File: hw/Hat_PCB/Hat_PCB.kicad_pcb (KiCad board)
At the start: 4 copper layers, 65 x 56 mm, 18 parts, among them J3 40HAT, J6 CONN_02X02, J9 CONN_01X02, Q1 DMG2305UX, Q2 DMMT5401, U2 CAT24C32

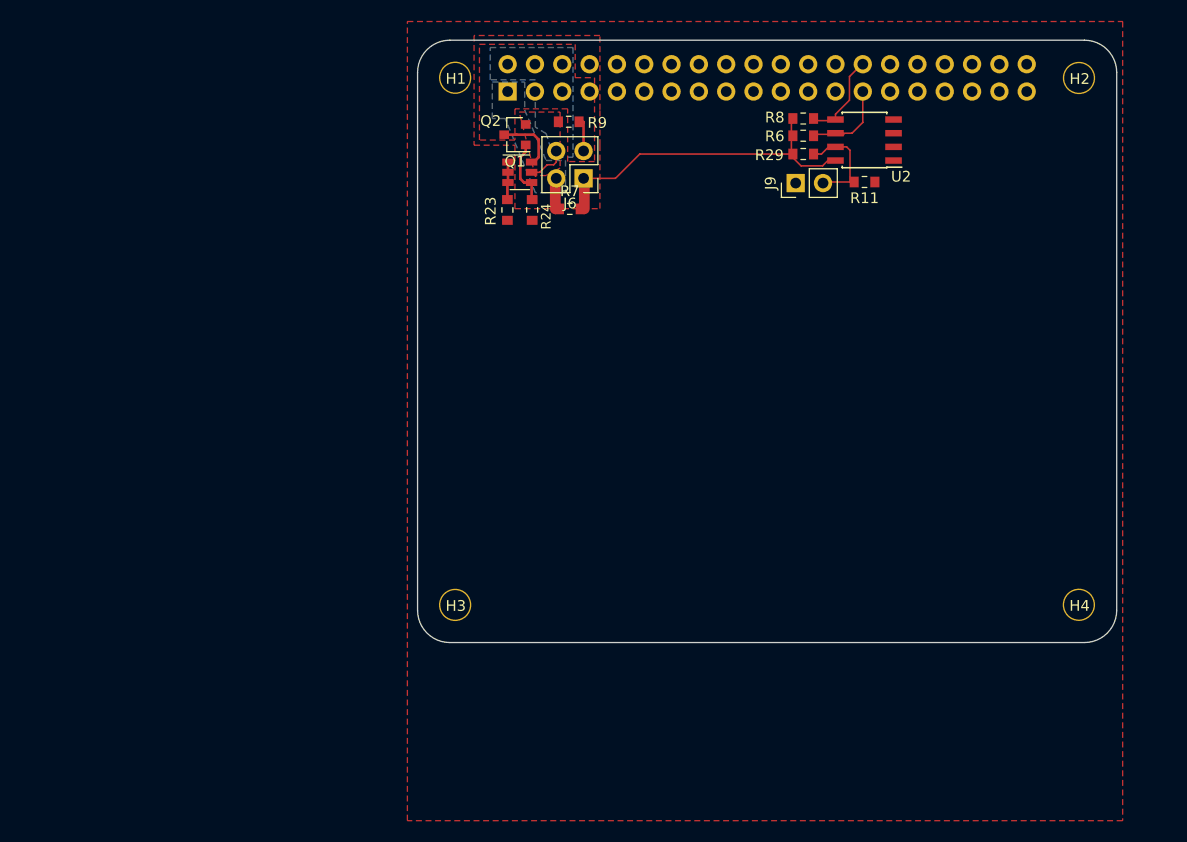
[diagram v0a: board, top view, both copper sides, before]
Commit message: Schematic mostly done, started prelim layout
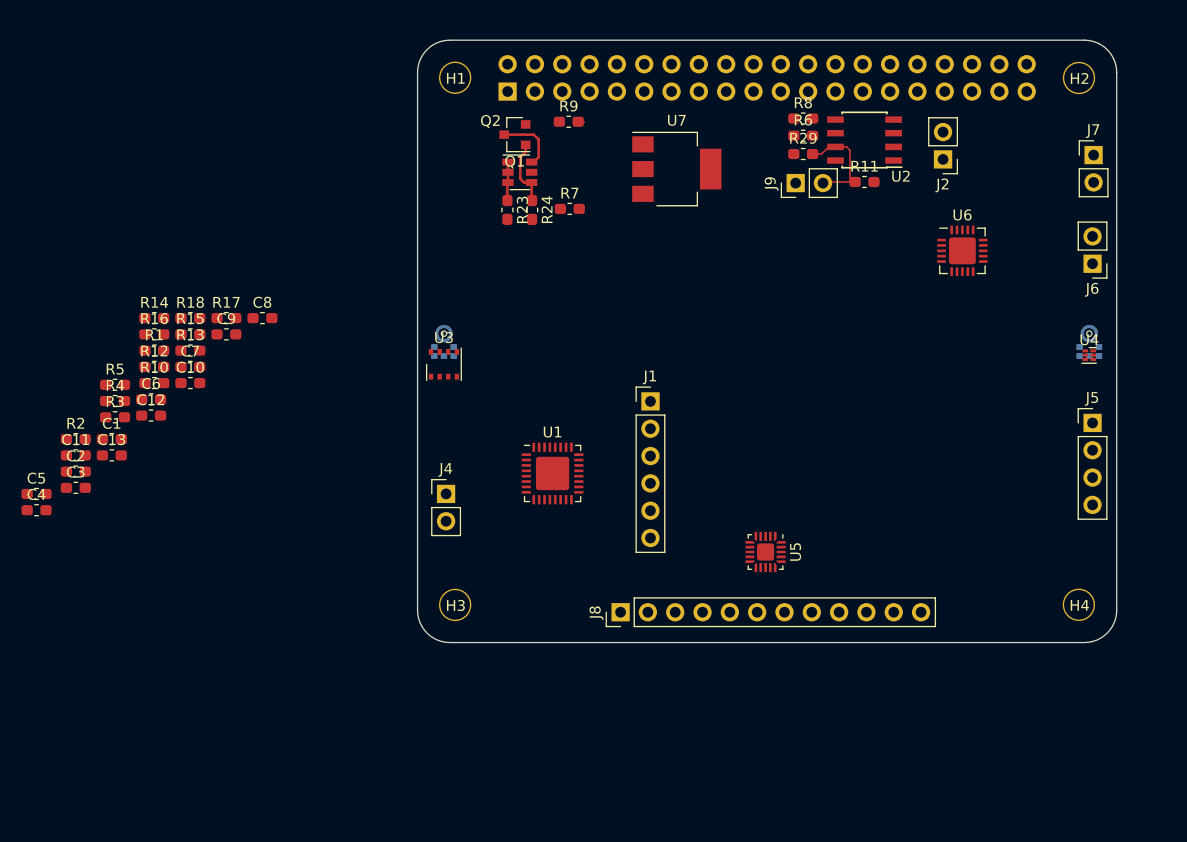
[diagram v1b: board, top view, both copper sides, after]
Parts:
- added C1: 10uF, Capacitor_SMD:C_0603_1608Metric_Pad1.05x0.95mm_HandSolder, F.Cu at (50.1, 97.9)
- added C10: 0.1uF, Capacitor_SMD:C_0603_1608Metric_Pad1.05x0.95mm_HandSolder, F.Cu at (57.4, 92.7)
- added C11: 0.1uF, Capacitor_SMD:C_0603_1608Metric_Pad1.05x0.95mm_HandSolder, F.Cu at (46.8, 99.4)
- added C12: 10uF, Capacitor_SMD:C_0603_1608Metric_Pad1.05x0.95mm_HandSolder, F.Cu at (53.8, 95.7)
- added C13: 10uF, Capacitor_SMD:C_0603_1608Metric_Pad1.05x0.95mm_HandSolder, F.Cu at (50.1, 99.4)
- added C2: 0.1uF, Capacitor_SMD:C_0603_1608Metric_Pad1.05x0.95mm_HandSolder, F.Cu at (46.8, 100.9)
- added C3: 0.1uF, Capacitor_SMD:C_0603_1608Metric_Pad1.05x0.95mm_HandSolder, F.Cu at (46.8, 102.4)
- added C4: 10uF, Capacitor_SMD:C_0603_1608Metric_Pad1.05x0.95mm_HandSolder, F.Cu at (43.1, 104.5)
- added C5: 10uF, Capacitor_SMD:C_0603_1608Metric_Pad1.05x0.95mm_HandSolder, F.Cu at (43.1, 103.0)
- added C6: 0.1uF, Capacitor_SMD:C_0603_1608Metric_Pad1.05x0.95mm_HandSolder, F.Cu at (53.8, 94.2)
- added C7: 0.1uF, Capacitor_SMD:C_0603_1608Metric_Pad1.05x0.95mm_HandSolder, F.Cu at (57.4, 91.2)
- added C8: 0.1uF, Capacitor_SMD:C_0603_1608Metric_Pad1.05x0.95mm_HandSolder, F.Cu at (64.1, 86.7)
- added C9: 0.1uF, Capacitor_SMD:C_0603_1608Metric_Pad1.05x0.95mm_HandSolder, F.Cu at (60.8, 88.2)
- added J1: ATTINY_ICSP, Connector_PinHeader_2.54mm:PinHeader_1x06_P2.54mm_Vertical, F.Cu at (100.2, 94.4)
- added J2: I2C, Connector_PinHeader_2.54mm:PinHeader_1x02_P2.54mm_Vertical, F.Cu at (127.4, 71.9)
- added J4: RPi_Power, Connector_PinHeader_2.54mm:PinHeader_1x02_P2.54mm_Vertical, F.Cu at (81.2, 103.0)
- added J5: AUD_IN, Connector_PinHeader_2.54mm:PinHeader_1x04_P2.54mm_Vertical, F.Cu at (141.3, 96.4)
- added J7: OUT_SPK_R, Connector_PinHeader_2.54mm:PinHeader_1x02_P2.54mm_Vertical, F.Cu at (141.4, 71.5)
- added J8: CAP_TOUCH, Connector_PinHeader_2.54mm:PinHeader_1x12_P2.54mm_Vertical, F.Cu at (97.4, 114.0)
- added MK1: SPH0645LM4H-B, MIC_SPH0645LM4H-B, B.Cu at (81.0, 88.1)
- added MK2: SPH0645LM4H-B, MIC_SPH0645LM4H-B, B.Cu at (141.0, 88.1)
- added R1: 33R, Resistor_SMD:R_0603_1608Metric_Pad1.05x0.95mm_HandSolder, F.Cu at (54.1, 89.7)
- added R10: 10K, Resistor_SMD:R_0603_1608Metric_Pad1.05x0.95mm_HandSolder, F.Cu at (54.1, 92.7)
- added R12: 10K, Resistor_SMD:R_0603_1608Metric_Pad1.05x0.95mm_HandSolder, F.Cu at (54.1, 91.2)
- added R13: 68R, Resistor_SMD:R_0603_1608Metric_Pad1.05x0.95mm_HandSolder, F.Cu at (57.4, 89.7)
- added R14: 0R, Resistor_SMD:R_0603_1608Metric_Pad1.05x0.95mm_HandSolder, F.Cu at (54.1, 86.7)
- added R15: 0R, Resistor_SMD:R_0603_1608Metric_Pad1.05x0.95mm_HandSolder, F.Cu at (57.4, 88.2)
- added R16: 0R, Resistor_SMD:R_0603_1608Metric_Pad1.05x0.95mm_HandSolder, F.Cu at (54.1, 88.2)
- added R17: 75K, Resistor_SMD:R_0603_1608Metric_Pad1.05x0.95mm_HandSolder, F.Cu at (60.8, 86.7)
- added R18: 10K, Resistor_SMD:R_0603_1608Metric_Pad1.05x0.95mm_HandSolder, F.Cu at (57.4, 86.7)
- added R2: 33R, Resistor_SMD:R_0603_1608Metric_Pad1.05x0.95mm_HandSolder, F.Cu at (46.8, 97.9)
- added R3: 33R, Resistor_SMD:R_0603_1608Metric_Pad1.05x0.95mm_HandSolder, F.Cu at (50.4, 95.9)
- added R4: 3.9K, Resistor_SMD:R_0603_1608Metric_Pad1.05x0.95mm_HandSolder, F.Cu at (50.4, 94.4)
- added R5: 3.9K, Resistor_SMD:R_0603_1608Metric_Pad1.05x0.95mm_HandSolder, F.Cu at (50.4, 92.9)
- added U1: ATtiny87-MU, Package_DFN_QFN:QFN-32-1EP_5x5mm_P0.5mm_EP3.1x3.1mm, F.Cu at (91.1, 101.1)
- added U3: BME680, Package_LGA:Bosch_LGA-8_3x3mm_P0.8mm_ClockwisePinNumbering, F.Cu at (81.0, 91.0)
- added U4: TSL2591, Package_DFN_QFN:DFN-6_1.3x1.2mm_P0.4mm, F.Cu at (141.0, 90.1)
- added U5: MPR121QR2, Package_DFN_QFN:QFN-20-1EP_3x3mm_P0.45mm_EP1.6x1.6mm, F.Cu at (110.9, 108.4)
- added U6: TPA2016D2RTJR, Package_DFN_QFN:QFN-20-1EP_4x4mm_P0.5mm_EP2.5x2.5mm, F.Cu at (129.2, 80.4)
- added U7: NCP1117-3.3_SOT223, Package_TO_SOT_SMD:SOT-223-3_TabPin2, F.Cu at (102.7, 72.8)
- J6: value CONN_02X02 -> OUT_SPK_L; footprint Connector_PinHeader_2.54mm:PinHeader_2x02_P2.54mm_Vertical -> Connector_PinHeader_2.54mm:PinHeader_1x02_P2.54mm_Vertical
- J9: value CONN_01X02 -> EE_WP
- R11, R29: footprint Resistor_SMD:R_0603_1608Metric_Pad0.84x1.00mm_HandSolder -> Resistor_SMD:R_0603_1608Metric_Pad1.05x0.95mm_HandSolder
- R23: value 22 -> 10K; footprint Resistor_SMD:R_0603_1608Metric_Pad0.84x1.00mm_HandSolder -> Resistor_SMD:R_0603_1608Metric_Pad1.05x0.95mm_HandSolder
- R24: value 22 -> 47K; footprint Resistor_SMD:R_0603_1608Metric_Pad0.84x1.00mm_HandSolder -> Resistor_SMD:R_0603_1608Metric_Pad1.05x0.95mm_HandSolder
- R6: value 3.9K -> 33R; footprint Resistor_SMD:R_0603_1608Metric_Pad0.84x1.00mm_HandSolder -> Resistor_SMD:R_0603_1608Metric_Pad1.05x0.95mm_HandSolder
- R7: value DNP -> 33R; footprint Resistor_SMD:R_0603_1608Metric_Pad0.84x1.00mm_HandSolder -> Resistor_SMD:R_0603_1608Metric_Pad1.05x0.95mm_HandSolder
- R8: value 3.9K -> 10K; footprint Resistor_SMD:R_0603_1608Metric_Pad0.84x1.00mm_HandSolder -> Resistor_SMD:R_0603_1608Metric_Pad1.05x0.95mm_HandSolder
- R9: value DNP -> 10K; footprint Resistor_SMD:R_0603_1608Metric_Pad0.84x1.00mm_HandSolder -> Resistor_SMD:R_0603_1608Metric_Pad1.05x0.95mm_HandSolder
- moved J6 48.0 mm to (141.3, 81.6)
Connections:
- J3 pad 1: /P3V3_HAT -> /Pi_3V3
- J3 pad 12: Net-(J3-Pad12) -> /MIC_CLK
- J3 pad 17: Net-(J3-Pad17) -> /Pi_3V3
- J3 pad 2: /P5V_HAT -> +5V
- J3 pad 27: /ID_SD_EEPROM -> /ID_SD
- J3 pad 28: /ID_SC_EEPROM -> /ID_SC
- J3 pad 3: Net-(J3-Pad3) -> /SDA
- J3 pad 35: Net-(J3-Pad35) -> /MIC_WS
- J3 pad 38: Net-(J3-Pad38) -> /MIC_DO
- J3 pad 4: /P5V_HAT -> +5V
- J3 pad 5: Net-(J3-Pad5) -> /SCL
- J6 pad 1: /P3V3 -> Net-(J6-Pad1)
- J6 pad 2: /P3V3_HAT -> Net-(J6-Pad2)
- Q1 pad 2: /P5V_HAT -> +5V
- Q1 pad 3: /P5V -> /PSUP_5V
- Q2 pad 5: /P5V_HAT -> +5V
- Q2 pad 6: /P5V -> /PSUP_5V
- R29 pad 1: /P3V3 -> +3V3
- R6 pad 1: /P3V3 -> Net-(J3-Pad22)
- R6 pad 2: /ID_SD_EEPROM -> /PROG_RST_N
- R7 pad 1: /P3V3_HAT -> Net-(J3-Pad24)
- R7 pad 2: /P3V3 -> /SPI_CS_N
- R8 pad 1: /P3V3 -> +3V3
- R8 pad 2: /ID_SC_EEPROM -> /PROG_RST_N
- R9 pad 1: /P5V_HAT -> Net-(MK1-Pad2)
- R9 pad 2: /P5V -> GND
- U2 pad 5: /ID_SC_EEPROM -> /ID_SC
- U2 pad 6: /ID_SD_EEPROM -> /ID_SD
- U2 pad 8: /P3V3 -> +3V3
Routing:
- net /P3V3: track 31.3 -> 0.00 mm
- net /ID_SD_EEPROM: track 8.99 -> 0.00 mm
- net /P5V: track 8.71 -> 0.00 mm
- net /ID_SC_EEPROM: track 8.17 -> 0.00 mm
- net /PSUP_5V: track 0.00 -> 5.97 mm
- net /P5V_HAT: track 3.77 -> 0.00 mm
- net /P3V3_HAT: track 2.88 -> 0.00 mm
- removed copper zone on B.Cu, net /P3V3_HAT
- removed copper zone on F.Cu, net /P5V
- removed copper zone on B.Cu, net /P5V_HAT
- removed copper zone on F.Cu, net /P5V_HAT
- removed copper zone on F.Cu, net GND
- removed copper zone on In2.Cu, net GND
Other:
- copper layers 4 -> 2
- board text removed: "If you want to use an SMT 40-pin header, please move the top edge up by 0.5mm and locate the header in the same location as the current TH part."
- board text removed: "This is a HAT compatible PCB starting design based on the official Raspberry Pi specs at: https://github.com/raspberrypi/hats/blob/master/designguide.md Currently the camera slot and display cutout are not here. See the schematic for the details on the EEPROM and power setup. This board does have the correct components for powering the Pi via the HAT. If you need the Pi to provide 5V or 3.3V, ple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"

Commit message: Added RTC, changed layout a bit
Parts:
- removed R23, R29: 10K, Resistor_SMD:R_0603_1608Metric_Pad1.05x0.95mm_HandSolder
- removed R24: 47K, Resistor_SMD:R_0603_1608Metric_Pad1.05x0.95mm_HandSolder
- added BT1: Battery_Cell, Battery:BatteryHolder_Keystone_3000_1x12mm, B.Cu at (104.1, 111.9)
- added D1: BAV99, SOT23-3, F.Cu at (96.2, 92.9)
- added J10: AudioJack3, Connector_Audio:Jack_3.5mm_CUI_SJ1-3533NG_Horizontal, F.Cu at (119.5, 113.2)
- added J11: AudioJack3_Ground, Connector_Audio:Jack_3.5mm_CUI_SJ1-3533NG_Horizontal, F.Cu at (140.6, 97.7)
- added R19: 0R, Resistor_SMD:R_0603_1608Metric_Pad1.05x0.95mm_HandSolder, F.Cu at (47.6, 82.7)
- added R20: 75K, Resistor_SMD:R_0603_1608Metric_Pad1.05x0.95mm_HandSolder, F.Cu at (50.9, 82.7)
- added R21: 10K, Resistor_SMD:R_0603_1608Metric_Pad1.05x0.95mm_HandSolder, F.Cu at (54.3, 82.7)
- added U8: MPR121QR2, Package_DFN_QFN:QFN-20-1EP_3x3mm_P0.45mm_EP1.6x1.6mm, F.Cu at (111.0, 90.2)
- J1: value ATTINY_ICSP -> EE_WP; footprint Connector_PinHeader_2.54mm:PinHeader_1x06_P2.54mm_Vertical -> Connector_PinHeader_2.54mm:PinHeader_1x02_P2.54mm_Vertical
- J2: value I2C -> 40HAT; footprint Connector_PinHeader_2.54mm:PinHeader_1x02_P2.54mm_Vertical -> Connector_PinSocket_2.54mm:PinSocket_2x20_P2.54mm_Vertical
- J3: value 40HAT -> AVR-ISP-6; footprint Connector_PinSocket_2.54mm:PinSocket_2x20_P2.54mm_Vertical -> Connector_PinHeader_2.54mm:PinHeader_2x03_P2.54mm_Vertical
- J4: value RPi_Power -> I2C
- J5: value AUD_IN -> RPi_Power; footprint Connector_PinHeader_2.54mm:PinHeader_1x04_P2.54mm_Vertical -> Connector_PinHeader_2.54mm:PinHeader_1x02_P2.54mm_Vertical
- J6: value OUT_SPK_L -> AUD_IN; footprint Connector_PinHeader_2.54mm:PinHeader_1x02_P2.54mm_Vertical -> Connector_PinHeader_2.54mm:PinHeader_1x04_P2.54mm_Vertical
- J7: value OUT_SPK_R -> OUT_SPK_L
- J8: value CAP_TOUCH -> OUT_SPK_R; footprint Connector_PinHeader_2.54mm:PinHeader_1x12_P2.54mm_Vertical -> Connector_PinHeader_2.54mm:PinHeader_1x02_P2.54mm_Vertical
- J9: value EE_WP -> CAP_TOUCH; footprint Connector_PinHeader_2.54mm:PinHeader_1x02_P2.54mm_Vertical -> Connector_PinHeader_2.54mm:PinHeader_1x12_P2.54mm_Vertical
- Q1: value DMG2305UX -> DMMT5401; footprint Package_TO_SOT_SMD:SOT-23 -> Package_TO_SOT_SMD:SOT-23-6
- Q2: value DMMT5401 -> DMG2305UX; footprint Package_TO_SOT_SMD:SOT-23-6 -> Package_TO_SOT_SMD:SOT-23
- R11: value DNP -> 10K
- R12: value 10K -> 47K
- R13: value 68R -> 10K
- R14, R15: value 0R -> 10K
- R16: value 0R -> 68R
- R17: value 75K -> 0R
- R18: value 10K -> 0R
- R4: value 3.9K -> DNP
- R5: value 3.9K -> 10K
- R6, R7: value 33R -> 3.9K
- R8, R9: value 10K -> 33R
- U1: value ATtiny87-MU -> CAT24C32; footprint Package_DFN_QFN:QFN-32-1EP_5x5mm_P0.5mm_EP3.1x3.1mm -> Package_SO:SOIC-8_3.9x4.9mm_P1.27mm
- U2: value CAT24C32 -> ATtiny87-MU; footprint Package_SOIC:SOIC-8_3.9x4.9mm_P1.27mm -> Package_DFN_QFN:QFN-32-1EP_5x5mm_P0.5mm_EP3.1x3.1mm
- U3: value BME680 -> NCP1117-3.3_SOT223; footprint Package_LGA:Bosch_LGA-8_3x3mm_P0.8mm_ClockwisePinNumbering -> Package_TO_SOT_SMD:SOT-223-3_TabPin2
- U5: value MPR121QR2 -> BME680; footprint Package_DFN_QFN:QFN-20-1EP_3x3mm_P0.45mm_EP1.6x1.6mm -> Package_LGA:Bosch_LGA-8_3x3mm_P0.8mm_ClockwisePinNumbering
- U6: value TPA2016D2RTJR -> DS3231M; footprint Package_DFN_QFN:QFN-20-1EP_4x4mm_P0.5mm_EP2.5x2.5mm -> Package_SO:SOIC-16W_7.5x10.3mm_P1.27mm
- U7: value NCP1117-3.3_SOT223 -> TPA2016D2RTJR; footprint Package_TO_SOT_SMD:SOT-223-3_TabPin2 -> Package_DFN_QFN:QFN-20-1EP_4x4mm_P0.5mm_EP2.5x2.5mm
- moved J5 64.1 mm to (80.8, 75.1), turned to 180 degrees
- moved R8 58.5 mm to (57.1, 80.1)
- moved R11 57.8 mm to (62.5, 79.0)
- moved J4 55.1 mm to (125.6, 70.3)
- moved U7 45.8 mm to (130.9, 108.8)
- moved U2 43.5 mm to (89.4, 100.9)
- moved U1 42.6 mm to (121.2, 71.0), turned to 90 degrees
- moved J2 41.5 mm to (86.9, 63.1), turned to 90 degrees
- moved J8 40.8 mm to (131.7, 91.9), turned to 270 degrees
- moved J3 37.9 mm to (96.2, 102.3), turned to 0 degrees
- moved R9 37.1 mm to (56.5, 76.8)
- moved U5 34.7 mm to (81.0, 90.7)
- moved U6 31.5 mm to (107.8, 103.5)
- moved J7 31.4 mm to (126.0, 98.9), turned to 180 degrees
- moved J6 28.8 mm to (125.4, 105.6), turned to 0 degrees
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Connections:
- J1 pad 1: /PROG_MISO -> GND
- J1 pad 2: /PROG_CLK -> Net-(J1-Pad2)
- J2 pad 1: /ID_SD -> /Pi_3V3
- J2 pad 2: /ID_SC -> +5V
- J3 pad 1: /Pi_3V3 -> /PROG_MISO
- J3 pad 2: +5V -> +3V3
- J3 pad 3: /SDA -> /PROG_SCK
- J3 pad 4: +5V -> /PROG_MOSI
- J3 pad 5: /SCL -> /PROG_RST_N
- J4 pad 1: GND -> /ID_SD
- J4 pad 2: /PSUP_5V -> /ID_SC
- J5 pad 1: /AUD_IN_R+ -> GND
- J5 pad 2: /AUD_IN_R- -> /PSUP_5V
- J6 pad 1: Net-(J6-Pad1) -> /AUD_IN_R+
- J6 pad 2: Net-(J6-Pad2) -> /AUD_IN_R-
- J7 pad 1: Net-(J7-Pad1) -> /AUD_O_L+
- J7 pad 2: Net-(J7-Pad2) -> /AUD_O_L-
- J8 pad 1: Net-(J8-Pad1) -> /AUD_O_R+
- J8 pad 2: Net-(J8-Pad2) -> /AUD_O_R-
- J9 pad 1: GND -> Net-(J9-Pad1)
- Q1 pad 2: +5V -> Net-(Q1-Pad1)
- Q1 pad 3: /PSUP_5V -> Net-(Q1-Pad1)
- Q2 pad 1: Net-(Q2-Pad1) -> Net-(Q1-Pad4)
- Q2 pad 2: Net-(Q2-Pad1) -> +5V
- Q2 pad 3: Net-(Q2-Pad1) -> /PSUP_5V
- R1 pad 2: Net-(J3-Pad19) -> Net-(J2-Pad19)
- R10 pad 1: +3V3 -> Net-(Q1-Pad1)
- R10 pad 2: /ALS_INT -> GND
- R11 pad 1: Net-(J9-Pad2) -> +3V3
- R11 pad 2: GND -> /PROG_RST_N
- R12 pad 1: Net-(MK2-Pad2) -> Net-(Q1-Pad4)
- R12 pad 2: +3V3 -> GND
- R13 pad 1: Net-(MK1-Pad6) -> +3V3
- R13 pad 2: /MIC_DO -> /ALS_INT
- R14 pad 1: +3V3 -> Net-(MK1-Pad2)
- R14 pad 2: /AUD_SDN -> GND
- R15 pad 1: /AUD_IN_L- -> Net-(MK2-Pad2)
- R15 pad 2: /AUD_IN_R- -> +3V3
- R16 pad 1: /AUD_IN_R- -> Net-(MK1-Pad6)
- R16 pad 2: GND -> /MIC_DO
- R17 pad 1: Net-(R17-Pad1) -> +3V3
- R17 pad 2: GND -> /AUD_SDN
- R18 pad 1: +3V3 -> /AUD_IN_L-
- R18 pad 2: /CAP_IRQ -> /AUD_IN_R-
- R2 pad 2: Net-(J3-Pad21) -> Net-(J2-Pad21)
- R3 pad 2: Net-(J3-Pad23) -> Net-(J2-Pad23)
- R4 pad 1: +3V3 -> Net-(J1-Pad2)
- R4 pad 2: /ID_SD -> GND
- R5 pad 2: /ID_SC -> Net-(J1-Pad2)
- R6 pad 1: Net-(J3-Pad22) -> +3V3
- R6 pad 2: /PROG_RST_N -> /ID_SD
- R7 pad 1: Net-(J3-Pad24) -> +3V3
- R7 pad 2: /SPI_CS_N -> /ID_SC
- R8 pad 1: +3V3 -> Net-(J2-Pad22)
- R9 pad 1: Net-(MK1-Pad2) -> Net-(J2-Pad24)
- R9 pad 2: GND -> /SPI_CS_N
- U1 pad 1: Net-(U1-Pad1) -> GND
- U1 pad 2: Net-(U1-Pad2) -> GND
- U1 pad 3: /LED_DATA -> GND
- U1 pad 4: +3V3 -> GND
- U1 pad 5: GND -> /ID_SC
- U1 pad 6: Net-(U1-Pad6) -> /ID_SD
- U1 pad 7: Net-(U1-Pad7) -> Net-(J1-Pad2)
- U1 pad 8: Net-(U1-Pad8) -> +3V3
- U2 pad 1: GND -> Net-(U2-Pad1)
- U2 pad 2: GND -> Net-(U2-Pad2)
- U2 pad 3: GND -> /LED_DATA
- U2 pad 4: GND -> +3V3
- U2 pad 5: /ID_SC -> GND
- U2 pad 6: /ID_SD -> Net-(U2-Pad6)
- U2 pad 7: Net-(J9-Pad2) -> Net-(U2-Pad7)
- U2 pad 8: +3V3 -> Net-(U2-Pad8)
- U3 pad 3: /SDA -> +5V
- U5 pad 1: /CAP_IRQ -> GND
- U5 pad 2: /SCL -> +3V3
- U5 pad 4: GND -> /SCL
- U5 pad 5: Net-(C10-Pad1) -> +3V3
- U5 pad 6: GND -> +3V3
- U5 pad 7: Net-(R17-Pad1) -> GND
- U5 pad 8: Net-(J8-Pad1) -> +3V3
- U6 pad 1: /AUD_IN_L+ -> /RTC_32KHZ
- U6 pad 10: Net-(J7-Pad1) -> GND
- U6 pad 11: +3V3 -> GND
- U6 pad 12: +3V3 -> GND
- U6 pad 13: +3V3 -> GND
- U6 pad 14: /AUD_IN_R- -> Net-(BT1-Pad1)
- U6 pad 15: /AUD_IN_R+ -> /SDA
- U6 pad 16: Net-(U6-Pad16) -> /SCL
- U6 pad 2: /AUD_IN_L- -> +3V3
- U6 pad 3: GND -> /RTC_INT
- U6 pad 4: +3V3 -> /RTC_RST
- U6 pad 5: +3V3 -> GND
- U6 pad 6: Net-(J6-Pad1) -> GND
- U6 pad 7: Net-(J6-Pad2) -> GND
- U6 pad 9: Net-(J7-Pad2) -> GND
- U7 pad 1: GND -> /AUD_IN_L+
- U7 pad 2: +3V3 -> /AUD_IN_L-
- U7 pad 3: +5V -> GND
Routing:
- net Net-(J9-Pad2): track 9.58 -> 0.00 mm
- net Net-(Q1-Pad1): track 6.02 -> 0.00 mm
- net /PSUP_5V: track 5.97 -> 0.00 mm
- net Net-(Q2-Pad1): track 3.37 -> 0.00 mm
